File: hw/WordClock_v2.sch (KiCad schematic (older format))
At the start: 23 parts, among them M1 ESP-07, P1 5V_input, P2 WS2812b_Out, P3 UART, SW1 SWITCH_INV, U1 NCP1117ST33T3G, U2 DS3232, U3 SN74LVC1T45, U4 WS2812b

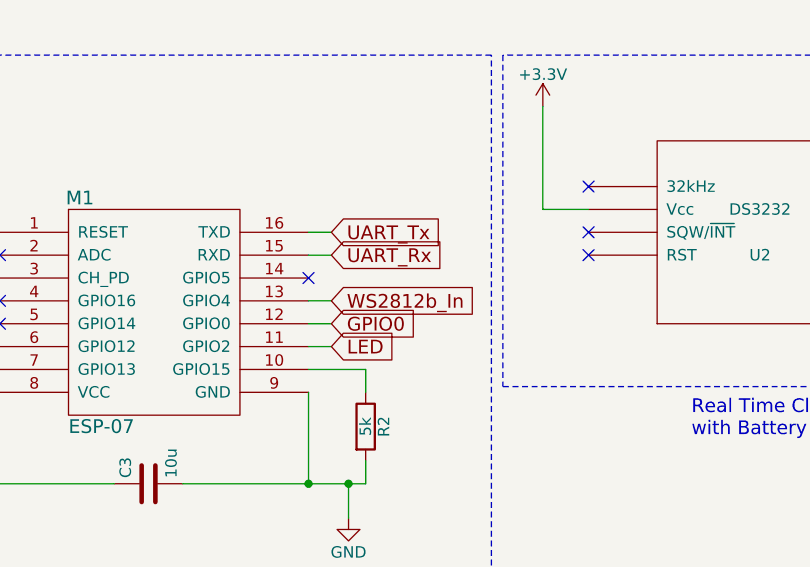
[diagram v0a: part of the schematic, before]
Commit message: Updated PCB to use RDX0/GPIO3 for WS2812b in order to use the NeoEps8266Dma800KbpsMethod of Makuna's NeoPixelBus library
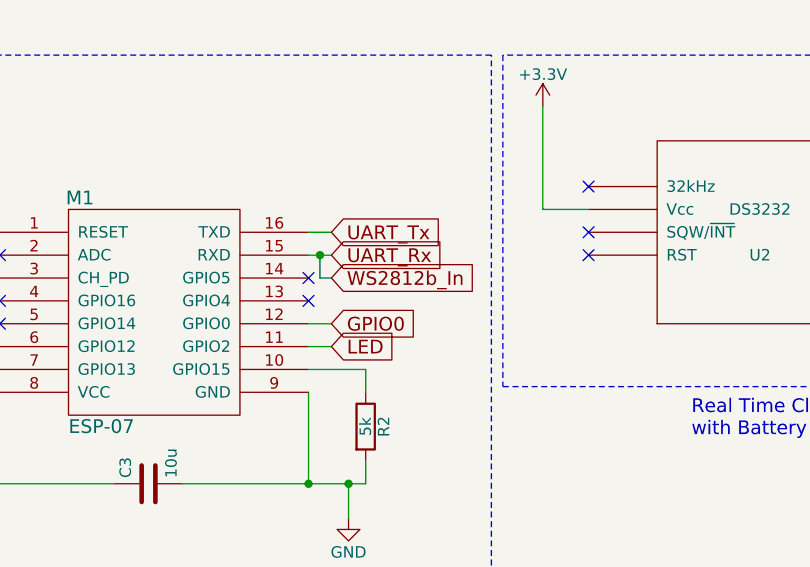
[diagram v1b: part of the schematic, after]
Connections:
- net UART_Rx: now also U3.3 (A)
- net WS2812b_In: no longer names the net of M1.13 (GPIO4)
- net WS2812b_In: no longer U3.3 (A)
- no-connect marks 8 -> 9
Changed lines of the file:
@@
 LIBS:memory
 LIBS:xilinx
-LIBS:special
 LIBS:microcontrollers
 LIBS:dsp
@@
 LIBS:contrib
 LIBS:valves
-LIBS:FabLibrary
 LIBS:WordClock_v2-cache
 EELAYER 25 0
@@
 	9450 1475 8400 1475
 Wire Wire Line
-	2850 3400 2750 3400
+	2750 3400 2850 3400
 Wire Wire Line
 	2750 3300 2850 3300
@@
 	1    0    0    -1
 $EndComp
-Text GLabel 2850 3600 2    60   Input ~ 0
+Text GLabel 2850 3500 2    60   Input ~ 0
 WS2812b_In
 NoConn ~ 2750 3500
@@
 NoConn ~ 1400 3600
 Wire Wire Line
-	2850 3600 2750 3600
-Wire Wire Line
 	5700 3200 5475 3200
 NoConn ~ 5475 3100
@@
 Wire Wire Line
 	9275 1375 9275 1275
+Wire Wire Line
+	2850 3500 2800 3500
+Wire Wire Line
+	2800 3500 2800 3400
+Connection ~ 2800 3400
+NoConn ~ 2750 3600
 $EndSCHEMATC

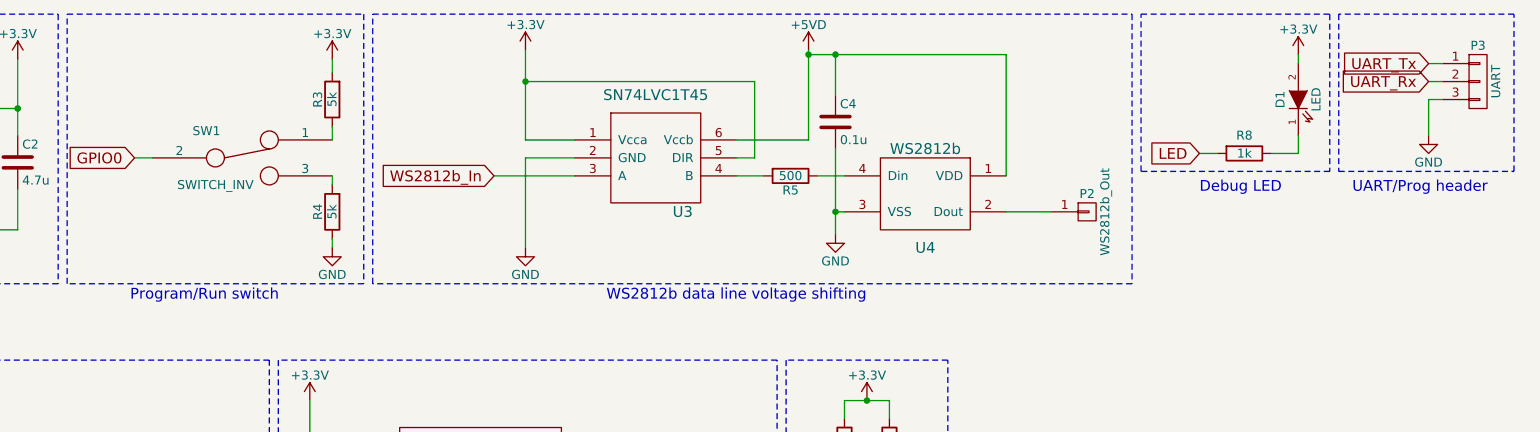
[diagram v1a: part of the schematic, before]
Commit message: Switched to diode-drop method of voltage conversion and changed from switch to push button for entering programming mode
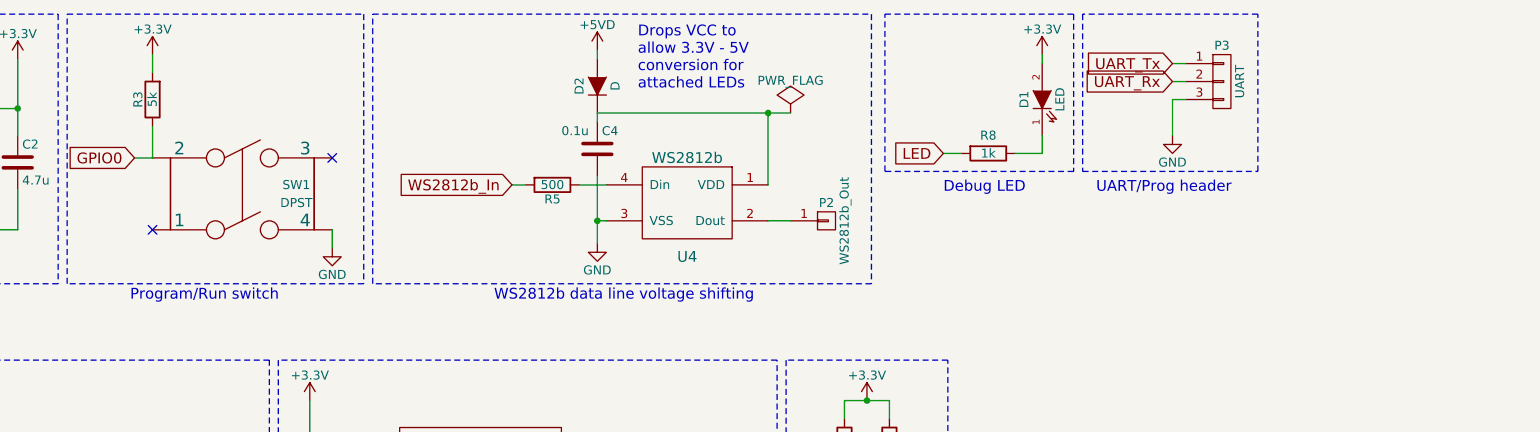
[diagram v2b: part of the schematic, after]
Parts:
- removed R4: 5k, FabLibrary:C_1206_HandSoldering_IainEdit, symbol R
- removed SW1: SWITCH_INV, FabLibrary:SlideSwitch_smd, symbol SWITCH_INV
- removed U3: SN74LVC1T45, FabLibrary:TI-DBV-SOT23_handsolder, symbol SN74LVC1T45
- added D2: D, IainPersonalLibrary:SOD-123F_HandSolder, symbol D
- added SW1: DPST, IainPersonalLibrary:FSM2JSMA_DPST_PushButton, symbol DPST
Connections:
- net +5VD: now also D2.2 (A); no longer C4.1, U4.1 (VDD)
- net GND: now also SW1.4
- net GPIO0: now also R3.1, SW1.2
- net UART_Rx: now also R5.2
- new net: C4.1, D2.1 (K), U4.1 (VDD)
- no-connect marks 9 -> 11
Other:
- note added: "Drops VCC to\nallow 3.3V - 5V \nconversion for\nattached LEDs"
- moved on the sheet: C4, D1, P2, P3, R3, R5, R8, U4
